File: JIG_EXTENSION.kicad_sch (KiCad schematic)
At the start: 53 parts, among them J1 Conn_01x03_Pin, J10 USB_B, J2 Conn_01x04_Pin, J3 Conn_01x07_Pin, J4 Conn_01x12_Socket, J5 Conn_01x12_Socket, J6 VIN, J7 618037231321, J8 Conn_01x18_Pin, J9 Conn_01x19_Pin, U1 ESP32-DEVKIT-V1, U2 CH340E, U3 AMS1117-3.3, U4 NCP1117DT50RKG, U5 SN74LVC1G3157DBVR, U6 SN74LVC1G3157DBVR, U7 SN74LVC1G3157DBVR, U8 SN74LVC1G3157DBVR

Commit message: ready to produce
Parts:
- removed D2: DIODE, Diode_SMD:D_SOD-323, symbol Diode:PMEG2020EJ
- removed J2: Conn_01x04_Pin, Connector_JST:JST_XH_S4B-XH-A_1x04_P2.50mm_Horizontal, symbol Connector:Conn_01x04_Pin
- removed L1: L, Inductor_SMD:L_0603_1608Metric, symbol Device:L
- removed U7, U8: SN74LVC1G3157DBVR, Package_TO_SOT_SMD:SOT-23-6, symbol SN74LVC1G3157DBVR:SN74LVC1G3157DBVR
- added C10, C9: 100nF, Capacitor_SMD:C_0603_1608Metric, symbol Device:C_Small
- added C11, C8: 18pF, Capacitor_SMD:C_0603_1608Metric, symbol Device:C_Small
- added C12: 1nF, Capacitor_SMD:C_0402_1005Metric, symbol Device:C_Small
- added C13: 100n, Capacitor_SMD:C_0603_1608Metric, symbol Device:C
- added C14: 1u, Capacitor_SMD:C_0603_1608Metric, symbol Device:C
- added D10, D11, D8, D9: LED, LED_SMD:LED_0805_2012Metric, symbol Device:LED
- added D2: SM712_SOT23, Package_TO_SOT_SMD:SOT-323_SC-70, symbol Diode:SM712_SOT23
- added D5: BZX84B4V7LT1, Package_TO_SOT_SMD:SOT-23, symbol TC-Power:D_Zener_SoT23
- added D6, D7: 6.8V CA, Diode_SMD:D_SMB, symbol Device:D_TVS
- added J11, J17, J21: VIN, TerminalBlock:TerminalBlock_Altech_AK300-2_P5.00mm, symbol Connector:Screw_Terminal_01x02
- added J12: Conn_01x02_Pin, Connector_PinHeader_2.54mm:PinHeader_1x02_P2.54mm_Horizontal, symbol Connector:Conn_01x02_Pin
- added J13, J14, J15, J16: Conn_01x02_Pin, Connector_PinHeader_2.54mm:PinHeader_1x02_P2.54mm_Vertical, symbol Connector:Conn_01x02_Pin
- added J18, J19, J20: Conn_01x04_Pin, Connector_PinHeader_2.54mm:PinHeader_1x04_P2.54mm_Horizontal, symbol Connector:Conn_01x04_Pin
- added J22: Conn_02x04_Odd_Even, Connector_PinHeader_2.54mm:PinHeader_2x04_P2.54mm_Horizontal, symbol Connector_Generic:Conn_02x04_Odd_Even
- added Q1: WST3325, Package_TO_SOT_SMD:SOT-23, symbol Device:Q_PMOS_GSD
- added R23: 100k, Resistor_SMD:R_0603_1608Metric, symbol Device:R_Small
- added R24, R25, R32, R33, R34: 10k, Resistor_SMD:R_0603_1608Metric, symbol Device:R_Small
- added R26, R27: 0, Resistor_SMD:R_0402_1005Metric, symbol Device:R
- added R28, R29: 2k8, Resistor_SMD:R_0603_1608Metric, symbol Device:R_Small
- added R30, R37, R40, R41: DNP, Resistor_SMD:R_0603_1608Metric, symbol Device:R_Small
- added R31, R42, R43, R44, R47, R48, R49, R50, R51, R55, R56: 0, Resistor_SMD:R_0603_1608Metric, symbol Device:R
- added R35, R36: 4k7, Resistor_SMD:R_0603_1608Metric, symbol Device:R_Small
- added R38, R39: 10, Resistor_SMD:R_1206_3216Metric, symbol Device:R_Small
- added R45: 2k, Resistor_SMD:R_0603_1608Metric, symbol Device:R_Small
- added R46: 1K, Resistor_SMD:R_0603_1608Metric, symbol Device:R_Small
- added R52: 10K, Resistor_SMD:R_0603_1608Metric, symbol Device:R_Small
- added R53, R54: 1K, Resistor_SMD:R_0603_1608Metric, symbol Device:R
- added U10: MCP2562-E-MF, Package_DFN_QFN:DFN-8-1EP_3x3mm_P0.65mm_EP1.55x2.4mm, symbol Interface_CAN_LIN:MCP2562-E-MF
- added U11: MAX13487EESAT, SOIC127P600X175-8N, symbol MAX13487EESAT:MAX13487EESAT
- added U9: MCP2515-xST, Package_SO:TSSOP-20_4.4x6.5mm_P0.65mm, symbol Interface_CAN_LIN:MCP2515-xST
- added Y1: 16MHz, Crystal:Crystal_SMD_Abracon_ABM8G-4Pin_3.2x2.5mm, symbol Device:Crystal_GND24
- J3: footprint Connector_JST:JST_XH_S7B-XH-A_1x07_P2.50mm_Horizontal -> Connector_PinSocket_2.54mm:PinSocket_1x07_P2.54mm_Vertical
- J7: footprint 618037231321 -> footprint:618037231321
- R21, R22: value 470 -> 1K
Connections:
- net AGND is gone; now on net GND: J4.1 (Pin_1), J5.1 (Pin_1), J5.12 (Pin_12), J7.27, J8.8 (Pin_8)
- net +12V: now also J21.2 (Pin_2), R44.1
- net +VS: now also R44.2
- net 3V3: now also C13.1, C14.1, D10.2 (A), D11.2 (A), J22.1 (Pin_1), R32.2, R33.2, R34.2, R35.2, R40.2, R41.2, U11.8 (VCC)
- net 3V3_B: now also U5.5 (VCC), U6.5 (VCC), C10.2, C9.2, J18.4 (Pin_4), J19.4 (Pin_4), J20.4 (Pin_4), R25.2, R46.2, U10.5 (Vio), U9.20 (VDD)
- net 5V0: now also R45.2, U10.3 (VDD)
- net A/D+: now also R42.2
- net B/D-: now also R43.2
- net CS: now also R24.2
- net DB_11: now also J13.1 (Pin_1)
- net DB_12: now also J14.1 (Pin_1)
- net DB_13: now also J15.1 (Pin_1)
- net DB_14: now also J16.1 (Pin_1)
- net DB_19: now also R50.2
- net DB_2: no longer J7.3, J9.3 (Pin_3)
- net DB_20: now also R47.1
- net DB_21: now also R48.1
- net DB_22: now also R49.1
- net GND: now also U5.2 (GND), U6.2 (GND), C10.1, C11.2, C12.2, C13.2, C14.2, C8.2, C9.1, D2.3 (common), D6.2 (A2), D7.2 (A2), D8.1 (K), D9.1 (K), J18.2 (Pin_2), J19.2 (Pin_2), J20.2 (Pin_2), J21.1 (Pin_1), J22.7 (Pin_7), R23.2, R36.1, R52.2, U10.2 (VSS), U10.9 (PAD), U11.5 (GND), U9.10 (VSS), Y1.2, Y1.4
- net MISO: now also U9.17 (SO)
- net MOSI: now also U9.16 (SI)
- net SCK: now also U9.14 (SCK)
- net UART_RS485_RX: now also R4.2, J22.5 (Pin_5), R34.1, R54.2, U11.4 (DI); no longer R3.2
- net UART_RS485_TX: now also R3.2, J22.3 (Pin_3), R32.1, R53.2, U11.1 (RO); no longer R4.2
- net at C5.1, R10.2, U4.3 (VI): now also D5.3 (K), Q1.2 (S)
- net VCU_SWDIO: now reaches U6.1 (B2)
- net VCU_SWDIO: now also J19.3 (Pin_3), R48.2
- net SWDIO: now reaches U6.3 (B1)
- net SWDIO: now also J18.3 (Pin_3), R50.1
- net SWDIO_OUT: now reaches U6.4 (A)
- net SWDIO_OUT: now also J20.3 (Pin_3)
- net SWD_SEL: now reaches U6.6 (S)
- net SWD_SEL: now also U5.6 (S), R51.2, R52.1
- net UART2_RX: now reaches R3.1, U1.6 (RX2)
- net UART2_TX: now reaches R4.1, U1.7 (TX2)
- net at F2.2: now also Q1.3 (D)
- net VCU_SWCLK: now reaches U5.1 (B2)
- net VCU_SWCLK: now also J19.1 (Pin_1), R49.2
- net SWCLK: now reaches U5.3 (B1)
- net SWCLK: now also J18.1 (Pin_1), R47.2
- net SWCLK_OUT: now reaches U5.4 (A)
- net SWCLK_OUT: now also J20.1 (Pin_1)
- net at U1.19 (D34): now also R51.1
- net at U1.9 (D18): now also R31.2
- net SPI_INT renamed CAN_INT
- net CAN_INT: now also U9.13 (~{INT})
- new net: D9.2 (A), R46.1
- new net: R35.1, R37.2, R38.2, R40.1, U11.6 (A)
- new net: D2.2 (A2), R26.2, R30.1, U10.7 (CANH)
- new net: R56.2, U10.4 (RXD)
- new net: C12.1, R28.2, R29.1
- new net: D5.1 (A), Q1.1 (G), R23.1
- new net: R36.2, R37.1, R39.2, R41.1, U11.7 (B)
- new net: R24.1, U9.18 (~{CS})
- new net: R25.1, U9.19 (~{RESET})
- new net: D10.1 (K), R53.1
- new net: D2.1 (A1), R27.2, R30.2, U10.6 (CANL)
- new net: D11.1 (K), R54.1
- new net: R55.2, U10.1 (TXD)
- new net: R33.1, U11.2 (~{RE}), U11.3 (~{SHDN})
- new net: D8.2 (A), R45.1
- new net CAN_H: J11.1 (Pin_1), J12.1 (Pin_1), J13.2 (Pin_2), J15.2 (Pin_2), R26.1, R28.1
- new net CAN_L: J11.2 (Pin_2), J12.2 (Pin_2), J14.2 (Pin_2), J16.2 (Pin_2), R27.1, R29.2
- new net CAN_OSC_1: C8.1, U9.9 (OSC1), Y1.1
- new net CAN_OSC_2: C11.1, U9.8 (OSC2), Y1.3
- new net CAN_SHDN: R31.1, U10.8 (SHDN)
- new net D+/A: D6.1 (A1), J17.1 (Pin_1), R38.1, R42.1
- new net D-/B: D7.1 (A1), J17.2 (Pin_2), R39.1, R43.1
- new net DB_3: J7.3, J9.3 (Pin_3)
- new net RX_CAN: R56.1, U9.2 (RXCAN)
- new net TX_CAN: R55.1, U9.1 (TXCAN)
- no-connect marks 5 -> 11
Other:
- note added: "(120R)"
- note added: "B1 set low to enable"
- note added: "CAN-MS 250k"
- note added: "FOR PSU"
- note added: "Lets try to avoid using the choke, But lets add the footprint in case of.."
- note added: "Main SWD"
- note added: "Power limit resistor"
- note added: "Reverse voltage protection"
- note added: "TVS is nice to have but a most if we add the choke to avoid high voltage spikes during a bus fault"
- note added: "VDS(max) = -20V VGS(max) = -+8V Drain I(max) = 5.5A RDS = ~{40mOhm G} threshold Voltage = -0.65V"
- moved on the sheet: C1, C2, C3, C4, C5, C6, C7, D1, D3, D4, J1, J10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

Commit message: done
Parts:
- removed C10, C9: 100nF, Capacitor_SMD:C_0603_1608Metric, symbol Device:C_Small
- removed C11, C8: 18pF, Capacitor_SMD:C_0603_1608Metric, symbol Device:C_Small
- removed C12: 1nF, Capacitor_SMD:C_0402_1005Metric, symbol Device:C_Small
- removed C13: 100n, Capacitor_SMD:C_0603_1608Metric, symbol Device:C
- removed C14: 1u, Capacitor_SMD:C_0603_1608Metric, symbol Device:C
- removed D1, D10, D11: LED, LED_SMD:LED_0805_2012Metric, symbol Device:LED
- removed D2: SM712_SOT23, Package_TO_SOT_SMD:SOT-323_SC-70, symbol Diode:SM712_SOT23
- removed D5: BZX84B4V7LT1, Package_TO_SOT_SMD:SOT-23, symbol TC-Power:D_Zener_SoT23
- removed D6, D7: 6.8V CA, Diode_SMD:D_SMB, symbol Device:D_TVS
- removed F2: C1F 2, Fuse:Fuse_1206_3216Metric, symbol Device:Fuse
- removed J1: Conn_01x03_Pin, Connector_JST:JST_XH_S3B-XH-A_1x03_P2.50mm_Horizontal, symbol Connector:Conn_01x03_Pin
- removed J10: USB_B, Connector_USB:USB_B_Lumberg_2411_02_Horizontal, symbol Connector:USB_B
- removed J11, J17, J21: VIN, TerminalBlock:TerminalBlock_Altech_AK300-2_P5.00mm, symbol Connector:Screw_Terminal_01x02
- removed J12: Conn_01x02_Pin, Connector_PinHeader_2.54mm:PinHeader_1x02_P2.54mm_Horizontal, symbol Connector:Conn_01x02_Pin
- removed J13, J14, J15, J16: Conn_01x02_Pin, Connector_PinHeader_2.54mm:PinHeader_1x02_P2.54mm_Vertical, symbol Connector:Conn_01x02_Pin
- removed J18, J19, J20: Conn_01x04_Pin, Connector_PinHeader_2.54mm:PinHeader_1x04_P2.54mm_Horizontal, symbol Connector:Conn_01x04_Pin
- removed J22: Conn_02x04_Odd_Even, Connector_PinHeader_2.54mm:PinHeader_2x04_P2.54mm_Horizontal, symbol Connector_Generic:Conn_02x04_Odd_Even
- removed J3: Conn_01x07_Pin, Connector_PinSocket_2.54mm:PinSocket_1x07_P2.54mm_Vertical, symbol Connector:Conn_01x07_Pin
- removed J4, J5: Conn_01x12_Socket, Connector_JST:JST_XH_S12B-XH-A-1_1x12_P2.50mm_Horizontal, symbol Connector:Conn_01x12_Socket
- removed J7: 618037231321, footprint:618037231321, symbol 618037231321:618037231321
- removed J8: Conn_01x18_Pin, Connector_PinHeader_2.54mm:PinHeader_1x18_P2.54mm_Vertical, symbol Connector:Conn_01x18_Pin
- removed J9: Conn_01x19_Pin, Connector_PinHeader_2.54mm:PinHeader_1x19_P2.54mm_Vertical, symbol Connector:Conn_01x19_Pin
- removed Q1: WST3325, Package_TO_SOT_SMD:SOT-23, symbol Device:Q_PMOS_GSD
- removed R1, R2, R3, R31, R4, R48, R49, R5, R50, R51, R55, R56, R7, R8, R9: 0, Resistor_SMD:R_0603_1608Metric, symbol Device:R
- removed R10: 5k, Resistor_SMD:R_0603_1608Metric, symbol Device:R_Small
- removed R21, R22, R53, R54: 1K, Resistor_SMD:R_0603_1608Metric, symbol Device:R
- removed R23: 100k, Resistor_SMD:R_0603_1608Metric, symbol Device:R_Small
- removed R24, R25, R34: 10k, Resistor_SMD:R_0603_1608Metric, symbol Device:R_Small
- removed R26, R27: 0, Resistor_SMD:R_0402_1005Metric, symbol Device:R
- removed R28, R29: 2k8, Resistor_SMD:R_0603_1608Metric, symbol Device:R_Small
- removed R30, R37, R40, R41: DNP, Resistor_SMD:R_0603_1608Metric, symbol Device:R_Small
- removed R35, R36: 4k7, Resistor_SMD:R_0603_1608Metric, symbol Device:R_Small
- removed R38, R39: 10, Resistor_SMD:R_1206_3216Metric, symbol Device:R_Small
- removed R45: 2k, Resistor_SMD:R_0603_1608Metric, symbol Device:R_Small
- removed R52: 10K, Resistor_SMD:R_0603_1608Metric, symbol Device:R_Small
- removed U1: ESP32-DEVKIT-V1, footprint:MODULE_ESP32_DEVKIT_V1, symbol ESP32-DEVKIT-V1:ESP32-DEVKIT-V1
- removed U10: MCP2562-E-MF, Package_DFN_QFN:DFN-8-1EP_3x3mm_P0.65mm_EP1.55x2.4mm, symbol Interface_CAN_LIN:MCP2562-E-MF
- removed U11: MAX13487EESAT, SOIC127P600X175-8N, symbol MAX13487EESAT:MAX13487EESAT
- removed U4: NCP1117DT50RKG, Package_TO_SOT_SMD:TO-252-2, symbol Regulator_Linear:NCP1117-5.0_TO252
- removed U5, U6: SN74LVC1G3157DBVR, Package_TO_SOT_SMD:SOT-23-6, symbol SN74LVC1G3157DBVR:SN74LVC1G3157DBVR
- removed U9: MCP2515-xST, Package_SO:TSSOP-20_4.4x6.5mm_P0.65mm, symbol Interface_CAN_LIN:MCP2515-xST
- removed Y1: 16MHz, Crystal:Crystal_SMD_Abracon_ABM8G-4Pin_3.2x2.5mm, symbol Device:Crystal_GND24
- added 3V3_ESP1, 3V3_USB1, 5V0, GND1: TP_V, TestPoint:TestPoint_Pad_D1.0mm, symbol Connector:TestPoint
- added C10, C9: 100nF, Capacitor_SMD:C_0603_1608Metric, symbol Device:C
- added C13, C14, C16: 100nF, Capacitor_SMD:C_0603_1608Metric, symbol Device:C_Small
- added C15, C8: 10uF, Capacitor_SMD:C_0603_1608Metric, symbol Device:C
- added C17: 1uF, Capacitor_SMD:C_0603_1608Metric, symbol Device:C_Small
- added D11, D5: SS14, Diode_SMD:D_SMA, symbol Diode:SS14
- added D12: PESD8V0L2BT-N, Package_TO_SOT_SMD:SOT-23, symbol TC-Transistors:PESD8V0L2BT-N
- added D13, D14, D6: SM712_SOT23, Package_TO_SOT_SMD:SOT-323_SC-70, symbol Diode:SM712_SOT23
- added D2, D7: 3V3_Z, Diode_SMD:D_SOD-323, symbol Device:D_Zener
- added IC1: MAX13487EESA+T, YZ-ICs:SOIC127P600X175-8N, symbol MAX13487EESA+T:MAX13487EESA+T
- added J2: Conn_01x10_Pin, Connector_PinHeader_2.54mm:PinHeader_1x10_P2.54mm_Horizontal, symbol Connector:Conn_01x10_Pin
- added J4: USB_B_Micro, Connector_USB:USB_Micro-B_Molex-105017-0001, symbol Connector:USB_B_Micro
- added J7: Conn_01x17_Pin, Connector_PinHeader_2.54mm:PinHeader_1x17_P2.54mm_Horizontal, symbol Connector:Conn_01x17_Pin
- added R1, R2: 22, Resistor_SMD:R_0402_1005Metric, symbol Device:R_Small
- added R10, R37, R38, R39, R40, R41: 0, Resistor_SMD:R_0603_1608Metric, symbol Device:R
- added R3, R4, R5, R7, R8, R9: 4K7, Resistor_SMD:R_0603_1608Metric, symbol Device:R_Small
- added R57, R58: 10K, Resistor_SMD:R_0603_1608Metric, symbol Device:R_Small
- added R61: DNP, Resistor_SMD:R_0402_1005Metric, symbol Device:R_Small
- added R63, R64: 10, Resistor_SMD:R_0603_1608Metric, symbol Device:R_Small
- added TP1, TP2: rs485_tx, TestPoint:TestPoint_Pad_D1.0mm, symbol Connector:TestPoint
- added U1: USBLC6-2SC6, Package_TO_SOT_SMD:SOT-23-6, symbol Power_Protection:USBLC6-2SC6
- added U11: TJA1051T/3, Package_SO:SOIC-8_3.9x4.9mm_P1.27mm, symbol Interface_CAN_LIN:TJA1051T-3
- added U12: K10-3U8S16D, YZ-Connector:K10-3U8S16D, symbol YZ_Connector:K10-3U8S16D
- added U5: L78L05_SOT89, Package_TO_SOT_SMD:SOT-89-3, symbol Regulator_Linear:L78L05_SOT89
- added U8: ESP32-S3-WROOM-1_Devkit, YZ-Connector:ESP32S3_DevkitPinHeader_1x22_P2.54mm_Vertical, symbol YZ_Connector:ESP32-S3-WROOM-1_Devkit
- C1, C4: value 100n -> 100nF; LCSC Part (none) -> C14663; MPN (none) -> CC0603KRX7R9BB104
- C2, C3: value 1u -> 1uF; LCSC Part (none) -> C15849; MPN (none) -> CL10A105KB8NNNC
- C5: value 10uF -> 0.33uF; footprint Capacitor_SMD:C_1206_3216Metric -> Capacitor_SMD:C_0805_2012Metric; LCSC Part (none) -> C1740; MPN (none) -> 0805B334K500NT
- C6: value 10uF -> 100nF; LCSC Part (none) -> C14663; MPN (none) -> CC0603KRX7R9BB104
- C7: LCSC Part (none) -> C96446; MPN (none) -> CL10A106MA8NRNC
- D3, D4, D8, D9: footprint LED_SMD:LED_0805_2012Metric -> LED_SMD:LED_0603_1608Metric; LCSC Part (none) -> C2286; MPN 0805RBD0070S01 -> KT-0603R
- J6: LCSC Part (none) -> C8475; MPN (none) -> WJ301V-5.0-02P-12-00A
- R11, R12, R13, R14, R15, R16, R17, R18, R19, R20, R42, R43, R44, R47, R6: LCSC Part (none) -> C21189; MPN (none) -> 0603WAF0000T5E
- R32, R33: value 10k -> 22; footprint Resistor_SMD:R_0603_1608Metric -> Resistor_SMD:R_0402_1005Metric; LCSC Part (none) -> C25092; MPN (none) -> 0402WGF220JTCE
- R46: value 1K -> 4K7; LCSC Part (none) -> C23162; MPN (none) -> 0603WAF4701T5E
- U2: LCSC Part (none) -> C99652; MPN (none) -> CH340E
- U3: LCSC Part (none) -> C6186; MPN (none) -> AMS1117-3.3
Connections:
- net AI5 is gone; now on net RS485_RX: R16.1
- net DB_1 is gone; now on net D-/B: R11.2
- net DB_2 is gone; now on net D+/A: R12.2
- net UART_QT_RX is gone; now on net CH340_TX: R19.2
- net UART_QT_TX is gone; now on net CH340_RX: R20.2
- net 3V3_B: now also C6.1, 3V3_USB1.1, C15.1, C8.1, D5.2 (A), U12.22 (VCC)
- net 5V0: now also 5V0.1, C10.1, C14.2, C16.1, C17.1, IC1.8 (VCC), J2.4 (Pin_4), R40.1, R5.1, R57.2, R58.2, R7.2, R8.1, U11.3 (VCC), U5.1 (OUT); no longer C6.1
- net D+/A: now also D12.1 (A1), R63.1; no longer R42.1
- net D-/B: now also D12.2 (A2), R64.1; no longer R43.1
- net GND: now also C10.2, C13.1, C14.1, C15.2, C16.2, C17.2, C8.2, C9.2, D12.3 (A3), D13.3 (common), D14.3 (common), D2.2 (A), D6.3 (common), D7.2 (A), GND1.1, IC1.5 (GND), J2.1 (Pin_1), J4.5 (GND), J4.6 (Shield), J7.16 (Pin_16), J7.7 (Pin_7), R9.2, U1.2 (GND), U11.2 (GND), U11.8 (S), U12.21 (GND), U12.9 (AGND), U5.2 (GND), U8.22 (GND), U8.23 (GND), U8.24 (GND), U8.44 (GND)
- net at D4.1 (K): now also R4.2
- net USB_VBUS: now reaches C1.1, C2.1, U3.3 (VI)
- net USB_VBUS: now also J4.1 (VBUS), U1.5 (VBUS)
- net 12V: now reaches C5.1
- net 12V: now also C9.1, D11.1 (K), J7.17 (Pin_17), U5.3 (IN)
- net at R6.2: now also U8.4 (IO4)
- net K10_RX: now reaches R18.1
- net K10_RX: now also U12.16 (TX)
- net at R18.2: now also U8.11 (IO18); no longer U2.2 (UD-)
- net at D3.1 (K): now also R3.2
- net K10_TX: now reaches R17.1
- net K10_TX: now also U12.15 (RX)
- net CH340_RX: now reaches U2.9 (RXD)
- net CH340_RX: now also D13.2 (A2), R4.1; no longer R20.1
- net at R17.2: now also U8.10 (IO17); no longer U2.1 (UD+)
- net CH340_TX: now reaches U2.8 (TXD)
- net CH340_TX: now also D13.1 (A1), R3.1; no longer R19.1
- net at R33.1: now also IC1.4 (DI), R57.1, TP2.1
- net at D8.2 (A): now also R5.2
- net +12V: no longer names the net of J6.2 (Pin_2)
- net +12V: now also D11.2 (A); no longer R44.1
- net +VS: no longer names the net of R44.2
- net +VS: now also U12.6 (AIN6)
- net 3V3 renamed RS485_RX
- net RS485_RX: no longer R33.2
- net AI0 renamed D-
- net D-: now also J7.10 (Pin_10)
- net AI1 renamed D+
- net D+: now also J7.11 (Pin_11)
- net AI2 renamed C_H
- net C_H: now also J7.12 (Pin_12)
- net AI3 renamed C_L
- net C_L: now also J7.13 (Pin_13)
- net AI4 renamed RS485_TX
- net RS485_TX: now also R33.2
- net A/D+: no longer names the net of R42.2
- net A/D+: now also U12.4 (AIN4)
- net B/D-: no longer names the net of R43.2
- net B/D-: now also U12.5 (AIN5)
- net DB_20 renamed 3V3_ANT
- net 3V3_ANT: now also J2.6 (Pin_6)
- net DB_5 renamed CAN_500_H
- net CAN_500_H: now also D6.1 (A1), U11.7 (CANH)
- net DB_7 renamed CAN_500_L
- net CAN_500_L: now also D6.2 (A2), U11.6 (CANL)
- net DB_8: no longer names the net of R15.2
- net DB_8: now also U8.8 (IO15)
- net DB_9: no longer names the net of R16.2
- net DB_9: now also U8.9 (IO16)
- net MISO renamed EN
- net EN: now also D14.1 (A1), J7.3 (Pin_3)
- net SWCLK: no longer names the net of R47.2
- net SWCLK: now also U12.7 (AIN7)
- net UART_RS485_TX: no longer names the net of R32.1
- net UART_RS485_TX: now also IC1.1 (RO), R58.1, TP1.1
- new net: IC1.6 (A), R61.2, R63.2, R8.2
- new net: R41.2, U12.3 (AIN3)
- new net: R39.2, U12.1 (AIN1)
- new net: R40.2, U12.2 (AIN2)
- new net: J4.2 (D-), R2.2
- new net: J4.3 (D+), R1.2
- new net: IC1.2 (~{RE}), IC1.3 (~{SHDN}), R7.1
- new net: IC1.7 (B), R61.1, R64.2, R9.1
- new net: R38.1, U8.36 (IO39)
- new net: R37.1, U8.37 (IO40)
- new net: R10.2, U8.5 (IO5)
- new net: R2.1, U1.4 (I/O2)
- new net: R1.1, U1.6 (I/O1)
- new net 3V3_AWS: J2.2 (Pin_2), R41.1
- new net 3V3_LDO: J2.10 (Pin_10), R43.1
- new net 3V3_OUT_ESP: 3V3_ESP1.1, C13.2, U11.5 (VIO), U8.1 (3V3), U8.2 (3V3)
- new net 4V0: J2.8 (Pin_8), R42.1
- new net 4V7_BOOST: J2.9 (Pin_9), R44.1
- new net 5V0_BUCK: J2.5 (Pin_5), R39.1
- new net 5V_ESP32: U8.21 (5V0)
- new net ADC_I: J7.15 (Pin_15)
- new net CAN_RXD: R38.2, U11.4 (RXD)
- new net CAN_TXD: R37.2, U11.1 (TXD)
- new net EBL: J2.3 (Pin_3)
- new net IBL: J2.7 (Pin_7)
- new net IGN: D2.1 (K), J7.8 (Pin_8), U8.19 (IO13)
- new net IM: D7.1 (K), J7.9 (Pin_9), U8.18 (IO12)
- new net IO0: D14.2 (A2), J7.4 (Pin_4), R10.1
- new net IO_E: J7.14 (Pin_14)
- new net NTC: J7.5 (Pin_5)
- new net RXD0: J7.1 (Pin_1), R19.1
- new net TXD0: J7.2 (Pin_2), R20.1
- new net USB_DM: U1.3 (I/O2), U2.2 (UD-)
- new net USB_DP: U1.1 (I/O1), U2.1 (UD+)
- new net VBAT: D5.1 (K), J7.6 (Pin_6)
- no-connect marks 11 -> 41
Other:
- note added: "120 Ohm"
- note added: "CAN-MS 500k"
- note added: "RS485 input voltage is 4.75 which hits the edge of internal battery booster's output, so route it to 5v_buck to enhance the stability"
- note removed: "(120R)"
- note removed: "B1 set low to enable"
- note removed: "CAN-MS 250k"
- note removed: "FOR PSU"
- note removed: "Main SWD"
- note removed: "Power limit resistor"
- moved on the sheet: C1, C2, C3, C4, C5, D3, D4, D8, D9, J6, R46, U2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

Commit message: modified 5V0
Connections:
- net 5V0: no longer J2.4 (Pin_4), R40.1
- new net 5V0_I: J2.4 (Pin_4), R40.1
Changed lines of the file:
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@@
 		)
 	)
-	(label "5V0"
+	(label "5V0_I"
 		(at 321.31 52.07 180)
 		(fields_autoplaced yes)
@@
 		)
 	)
-	(label "5V0"
+	(label "5V0_I"
 		(at 60.96 241.3 180)
 		(fields_autoplaced yes)
@@
 		)
 		(property "Value" "10K"
-			(at 228.6 255.27 0)
+			(at 238.506 251.968 0)
 			(effects
 				(font

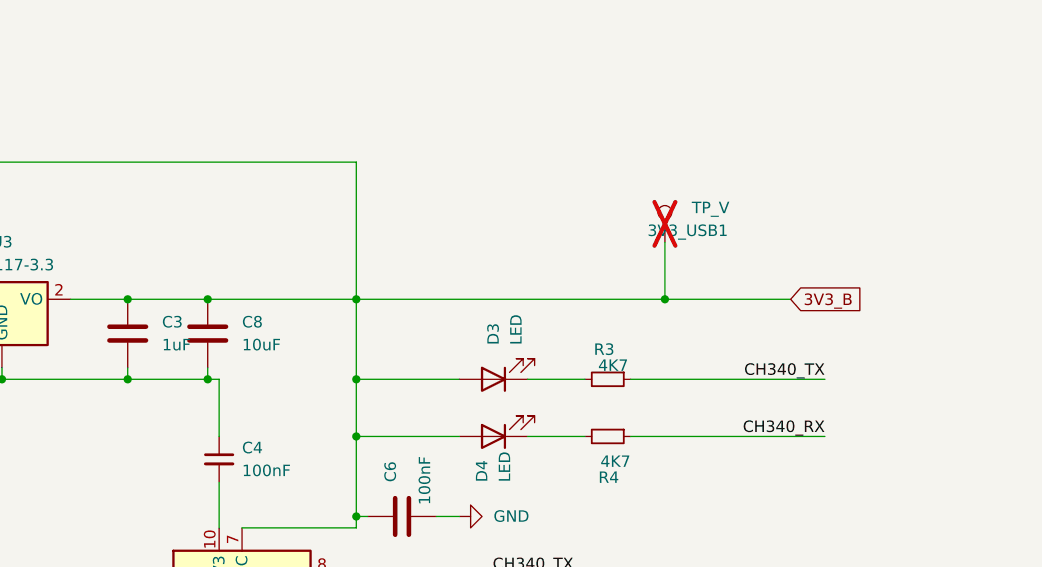
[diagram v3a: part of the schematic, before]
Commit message: added note on sch for 3v3_B
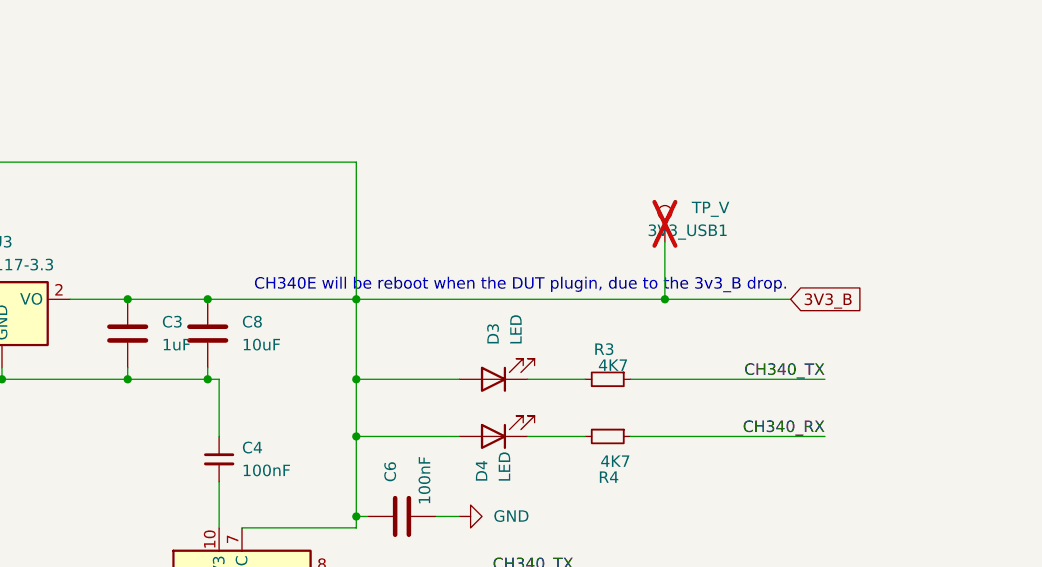
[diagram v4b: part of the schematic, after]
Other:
- note added: "CH340E will be reboot when the DUT plugin, due to the 3v3_B drop."
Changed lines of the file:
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@@
+		)
+	)
+	(text "CH340E will be reboot when the DUT plugin, due to the 3v3_B drop."
+		(exclude_from_sim no)
+		(at 145.288 138.176 0)
+		(effects
+			(font
+				(size 1.27 1.27)
+			)
 		)
 	)
